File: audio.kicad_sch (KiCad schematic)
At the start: 18 parts, among them Q4 2SC1815, U10 LM386N-1

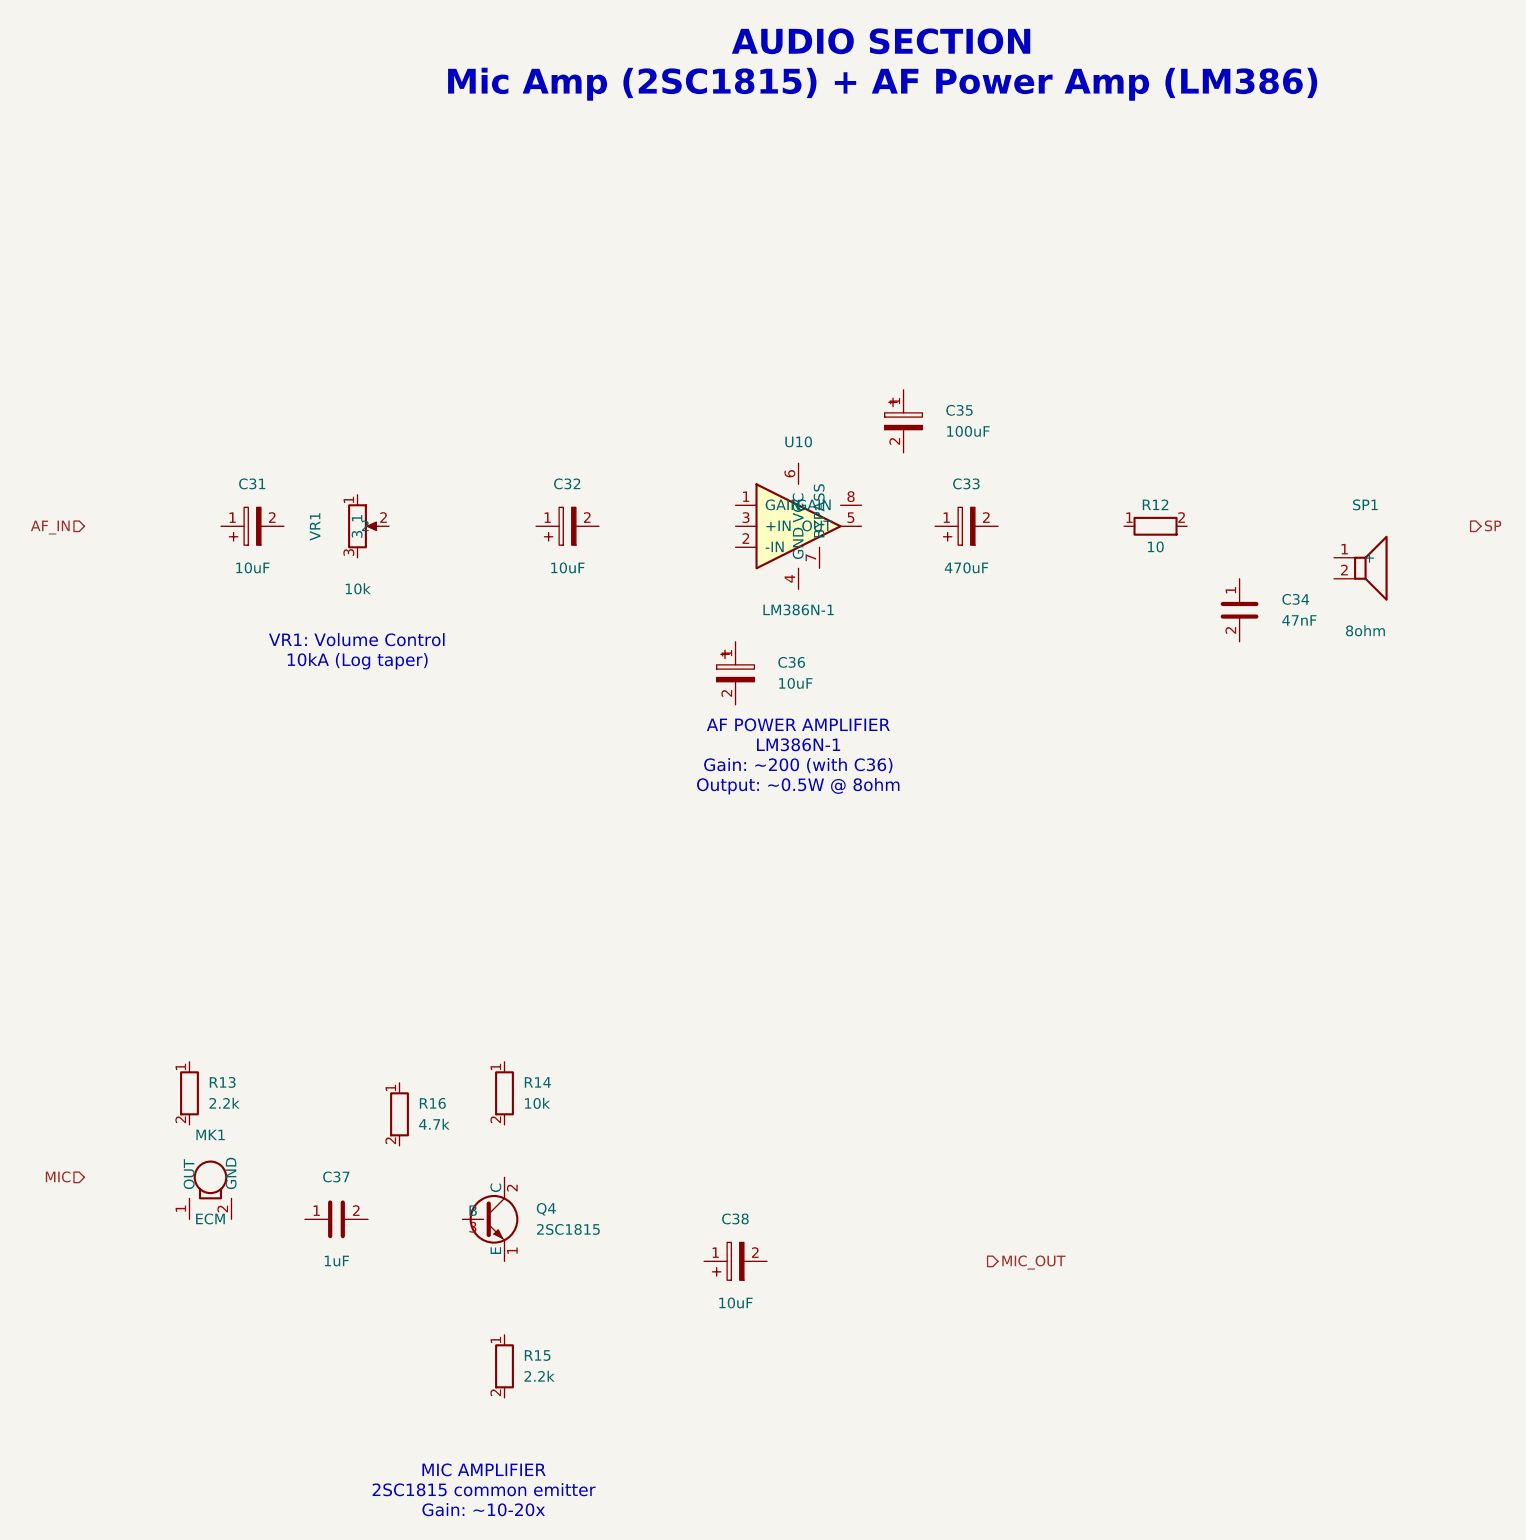
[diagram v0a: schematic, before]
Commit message: Add initial PCB layout with complete component placement
- Create 2-layer PCB (200x100mm) based on KiCad schematic import
- Place all components including Arduino Nano, Si5351, SA612 mixers, SSD1306 OLED
- Position audio amplifier (LM386), voltage regulators (7805/7808), crystal filters
- Add discrete components: resistors, capacitors, inductors, diodes, transistors
- Include connectors for power (DC jack), antenna, speaker, and microphone
- Update .gitignore to exclude fp-info-cache and backup directories
- Update schematic symbols for all circuit blocks (audio, BPF/LPF, control, IF filter, mixer/modulator, power amp, power supply)
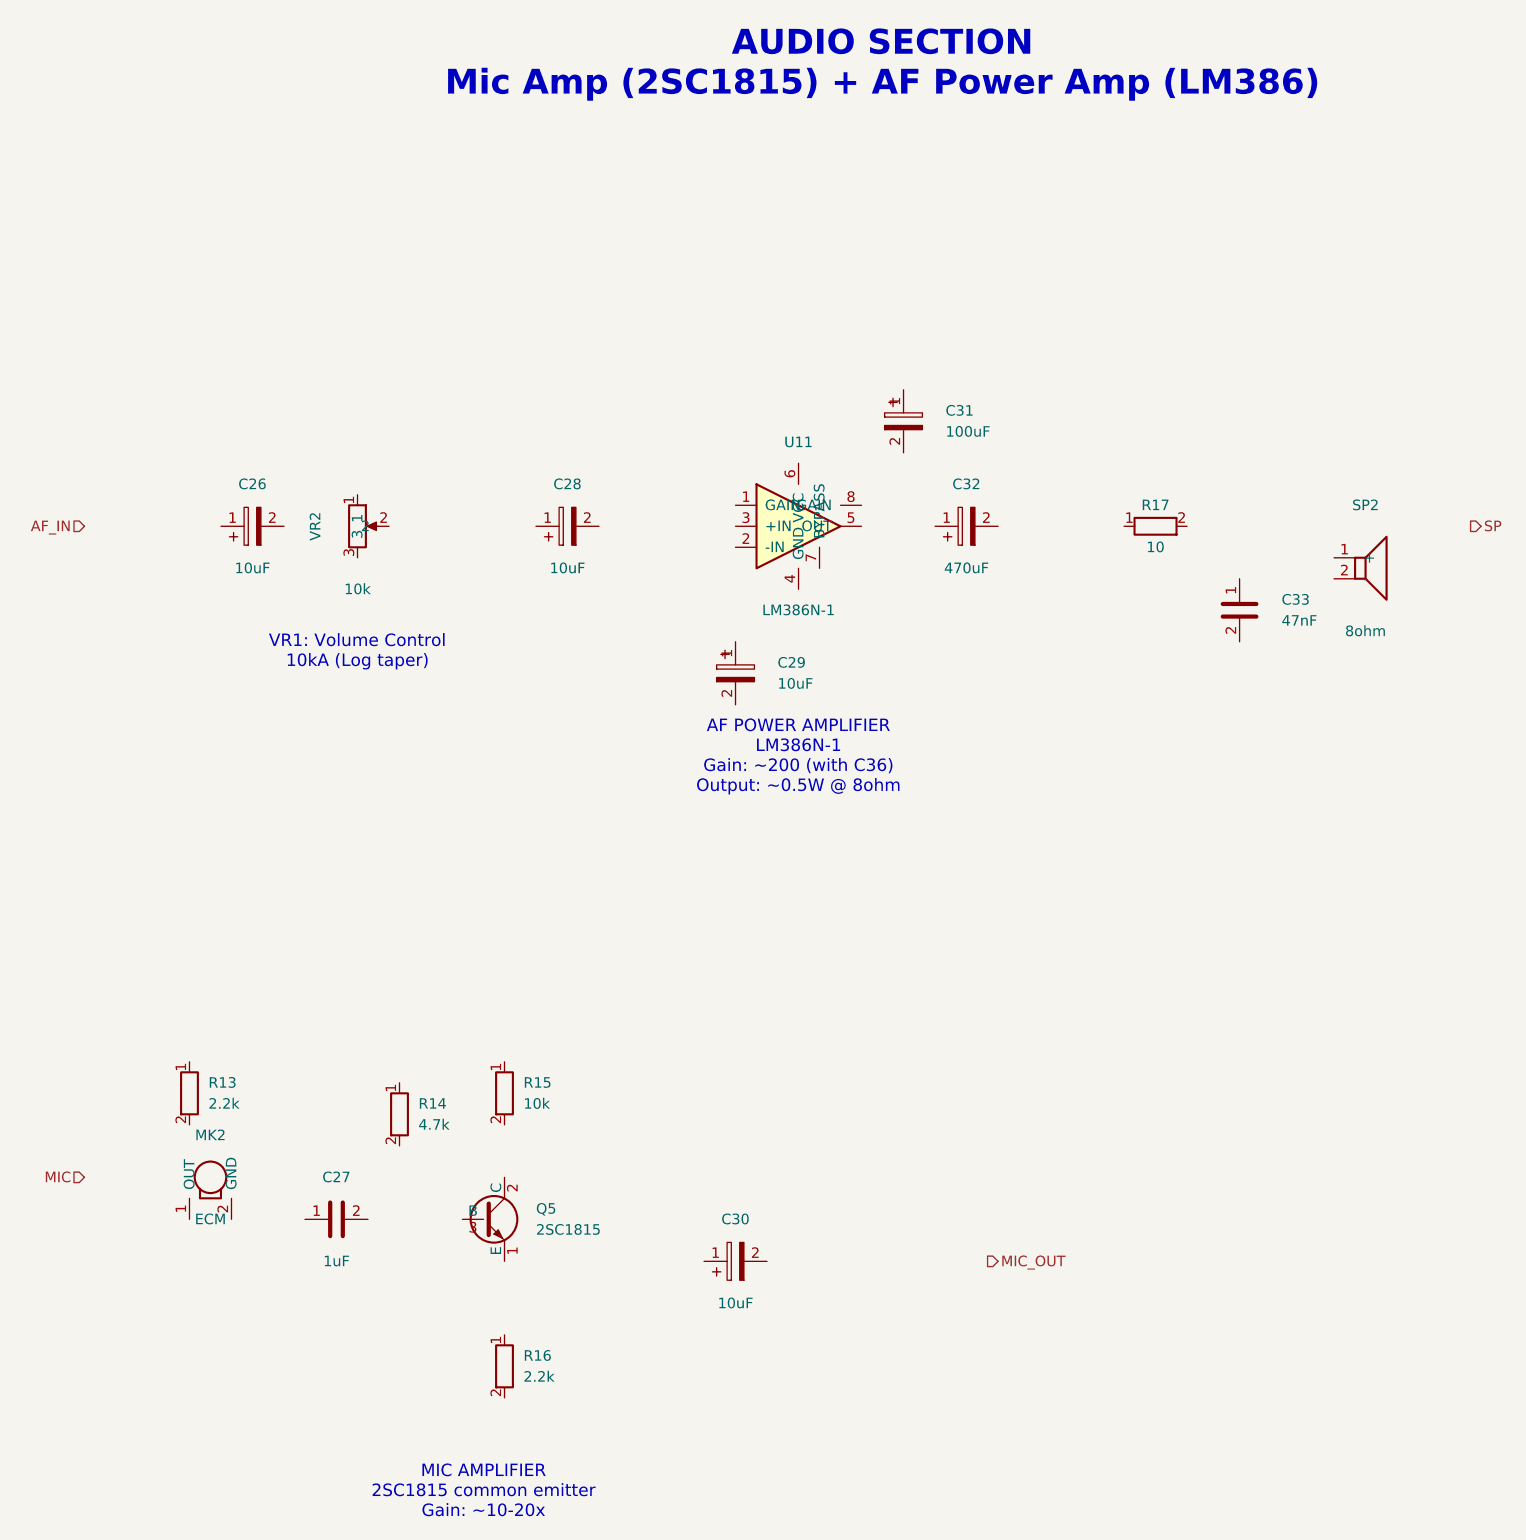
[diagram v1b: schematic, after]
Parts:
- removed C33: 470uF, symbol Device:CP
- removed C34: 47nF, symbol Device:C
- removed C35: 100uF, symbol Device:CP
- removed C36, C38: 10uF, symbol Device:CP
- removed C37: 1uF, symbol Device:C
- removed MK1: ECM, symbol Device:Microphone
- removed Q4: 2SC1815, symbol Transistor:2SC1815
- removed R12: 10, symbol Device:R
- removed SP1: 8ohm, symbol Device:Speaker
- removed U10: LM386N-1, symbol Amplifier:LM386
- removed VR1: 10k, symbol Device:R_POT
- added C26, C28, C29, C30: 10uF, Capacitor_THT:CP_Radial_D5.0mm_P2.50mm, symbol Device:CP
- added C27: 1uF, Capacitor_THT:CP_Radial_D5.0mm_P2.50mm, symbol Device:C
- added C33: 47nF, Capacitor_THT:C_Disc_D5.0mm_W2.5mm_P5.00mm, symbol Device:C
- added MK2: ECM, Connector_PinHeader_2.54mm:PinHeader_1x02_P2.54mm_Vertical, symbol Device:Microphone
- added Q5: 2SC1815, Package_TO_SOT_THT:TO-92_Inline, symbol Transistor:2SC1815
- added R17: 10, Resistor_THT:R_Axial_DIN0207_L6.3mm_D2.5mm_P10.16mm_Horizontal, symbol Device:R
- added SP2: 8ohm, Connector_PinHeader_2.54mm:PinHeader_1x02_P2.54mm_Vertical, symbol Device:Speaker
- added U11: LM386N-1, Package_DIP:DIP-8_W7.62mm, symbol Amplifier:LM386
- added VR2: 10k, Potentiometer_THT:Potentiometer_Alps_RK09K_Single_Vertical, symbol Device:R_POT
- C31: value 10uF -> 100uF; footprint (none) -> Capacitor_THT:CP_Radial_D5.0mm_P2.50mm
- C32: value 10uF -> 470uF; footprint (none) -> Capacitor_THT:CP_Radial_D8.0mm_P3.50mm
- R13: footprint (none) -> Resistor_THT:R_Axial_DIN0207_L6.3mm_D2.5mm_P10.16mm_Horizontal
- R14: value 10k -> 4.7k; footprint (none) -> Resistor_THT:R_Axial_DIN0207_L6.3mm_D2.5mm_P10.16mm_Horizontal
- R15: value 2.2k -> 10k; footprint (none) -> Resistor_THT:R_Axial_DIN0207_L6.3mm_D2.5mm_P10.16mm_Horizontal
- R16: value 4.7k -> 2.2k; footprint (none) -> Resistor_THT:R_Axial_DIN0207_L6.3mm_D2.5mm_P10.16mm_Horizontal
